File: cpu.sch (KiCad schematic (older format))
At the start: 4 parts, among them U2 MOS_8501

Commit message: Forgotten libs...
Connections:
- net labels added: PHI0
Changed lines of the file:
@@
 $Descr A4 11693 8268
 encoding utf-8
-Sheet 5 6
+Sheet 5 7
 Title ""
 Date ""
@@
 Wire Wire Line
 	4700 1930 4700 2795
+Text GLabel 4205 2395 0    50   Input ~ 0
+PHI0
 $EndSCHEMATC

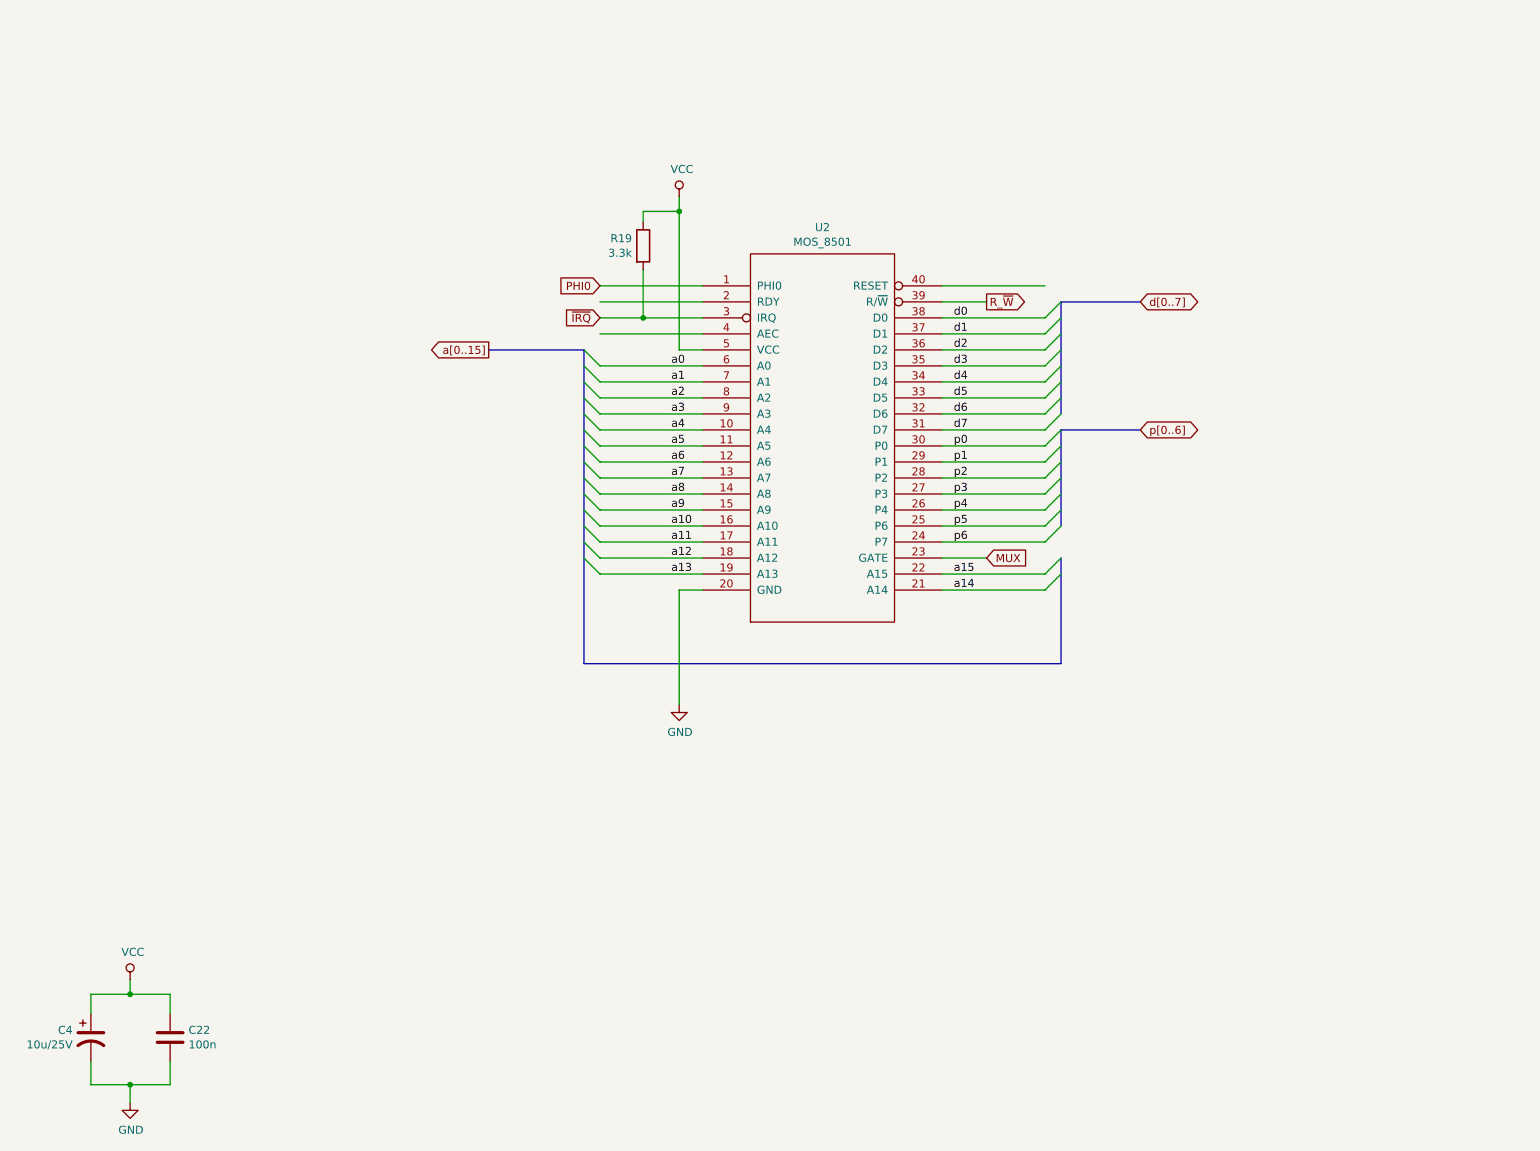
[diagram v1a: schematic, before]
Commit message: Add reset circuit
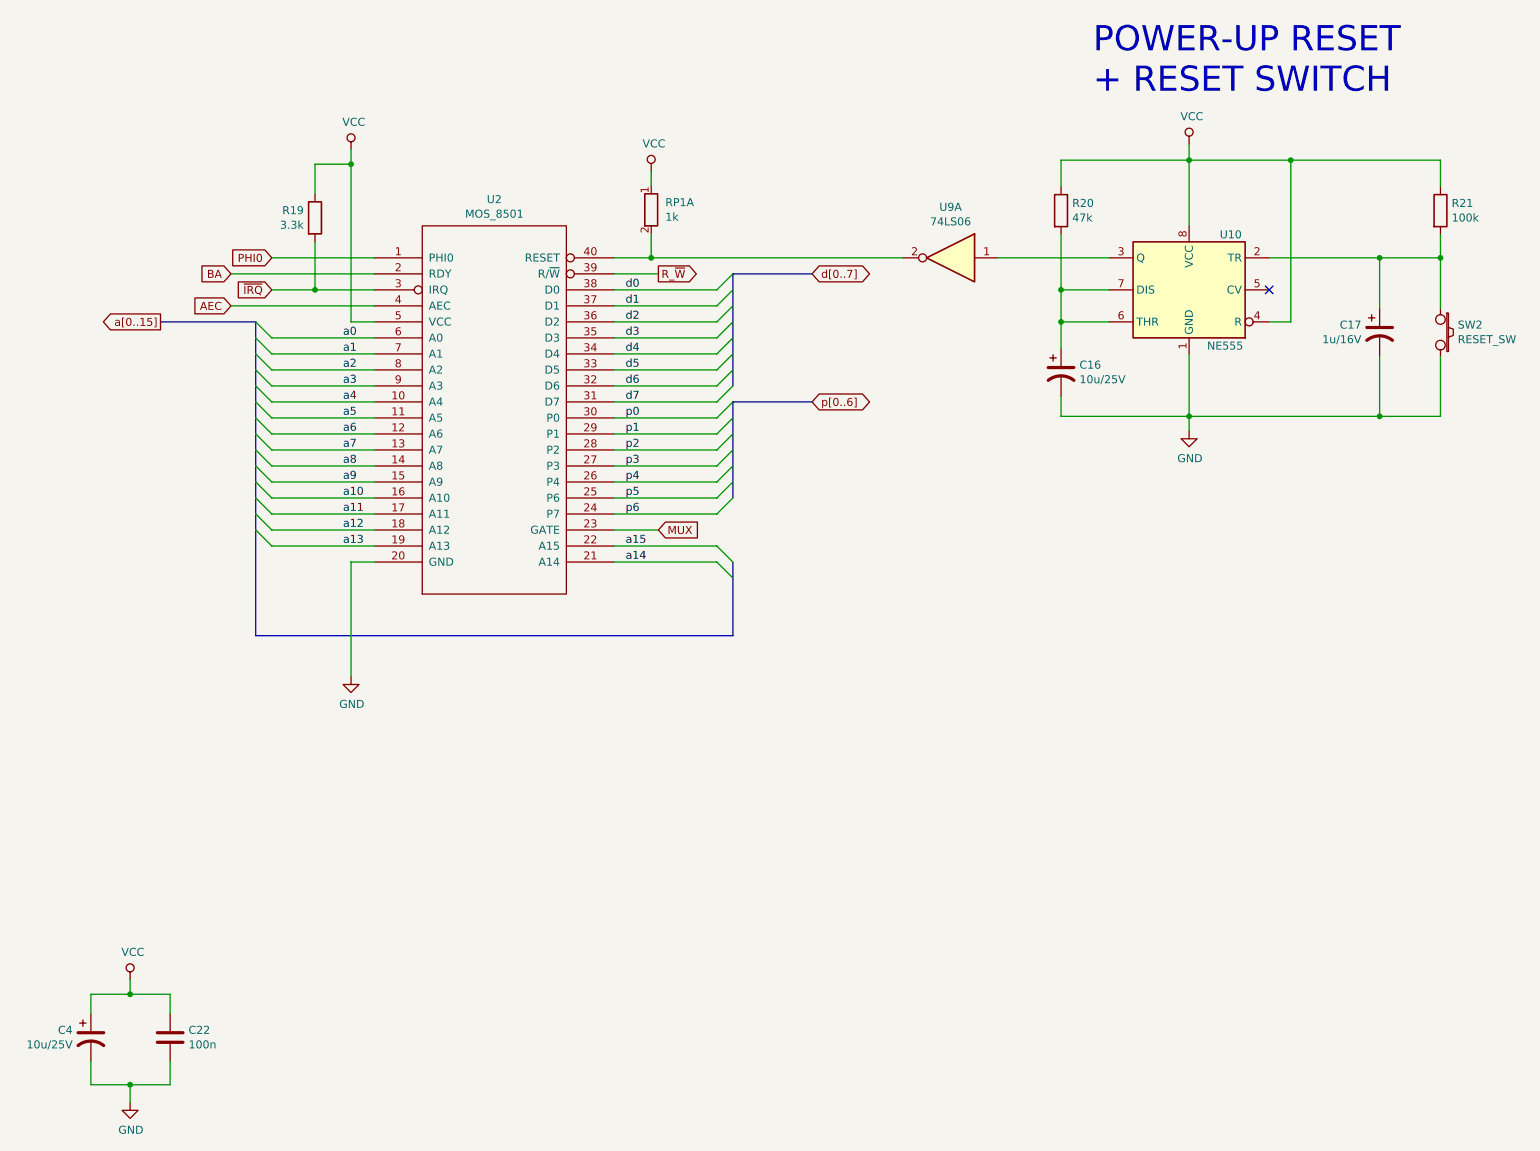
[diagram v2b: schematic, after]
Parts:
- added C16: 10u/25V, symbol Device:CP1
- added C17: 1u/16V, symbol Device:CP1
- added R20: 47k, symbol Device:R
- added R21: 100k, symbol Device:R
- added RP1: 1k, symbol r_pack05:R_Pack_5_Split
- added SW2: RESET_SW, symbol w_device:SW_PUSH
- added U10: NE555, symbol Timer:NE555
- added U9: 74LS06, symbol 74xx:74LS06
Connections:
- net labels added: AEC, BA
- wire segments 57 -> 88
- no-connect marks 0 -> 1
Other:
- note added: "POWER-UP RESET\n+ RESET SWITCH"
- moved on the sheet: R19, U2

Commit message: Connect Datassette signals to I/O pins
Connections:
- net p5 is gone; now on net p6: U2.25 (P6)
- net p6: no longer U2.24 (P7)
- new net p7: U2.24 (P7)
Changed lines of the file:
@@
 p4
 Text Label 4365 3720 0    50   ~ 0
-p5
+p6
 Text Label 4365 3820 0    50   ~ 0
-p6
+p7
 Text Label 2600 2720 0    50   ~ 0
 a0

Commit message: Add Serial Bus
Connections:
- net RESET: now reaches U10.3 (Q), U9.1
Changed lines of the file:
@@
 	5035 3120 5530 3120
 Text GLabel 5530 3120 2    50   BiDi ~ 0
-p[0..6]
+p[0..7]
 Text GLabel 4570 3920 2    50   Input ~ 0
 MUX
@@
 $EndComp
 Wire Wire Line
-	6695 2220 7385 2220
-Wire Wire Line
 	4295 2220 4525 2220
 Wire Wire Line
@@
 Text GLabel 1900 2520 0    50   Input ~ 0
 AEC
+Text GLabel 9325 3720 2    50   Output ~ 0
+RESET
+Wire Wire Line
+	6695 2220 6855 2220
+Wire Wire Line
+	6855 2220 6850 3720
+Wire Wire Line
+	6850 3720 9325 3720
+Connection ~ 6855 2220
+Wire Wire Line
+	6855 2220 7385 2220
 Wire Bus Line
 	5035 4120 5035 4580
